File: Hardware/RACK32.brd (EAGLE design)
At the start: 120 x 54 mm, 95 parts, among them IC1 MCP9808-MSOP8, IC2 ESPWROOM32, IC3 LM358D, IC4 W5500-LQFP, IC5 CP2102N-A01-GQFN24, J1 SPI-LCD, J10 microSD, J11 IO, J2 I2CBR, J3 USB-C-16P-16P, J4 DC IN, J6 PWR_LED, Q1 FDN340P, Q2 MMDT3904, U1 HY931147C-RJ45

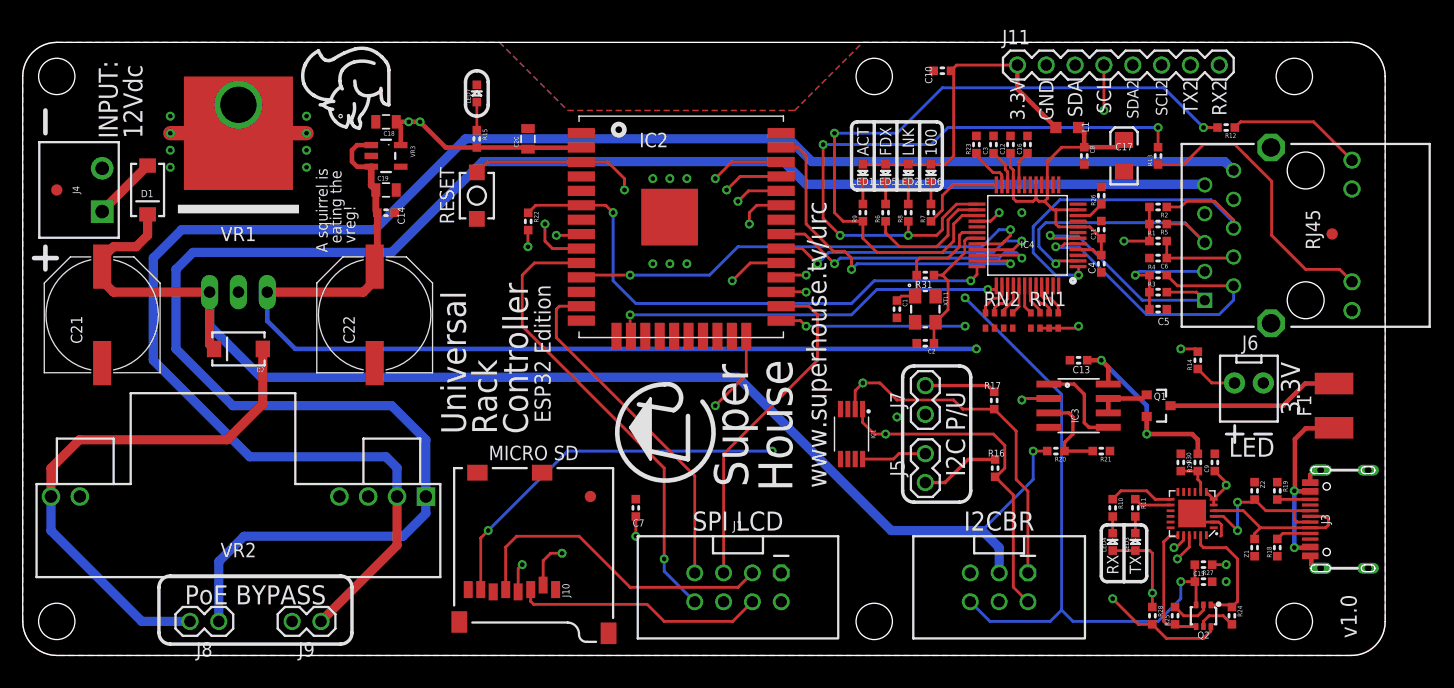
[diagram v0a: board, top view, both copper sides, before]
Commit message: Changed PTC to 1206 size. Replaced power LED header.
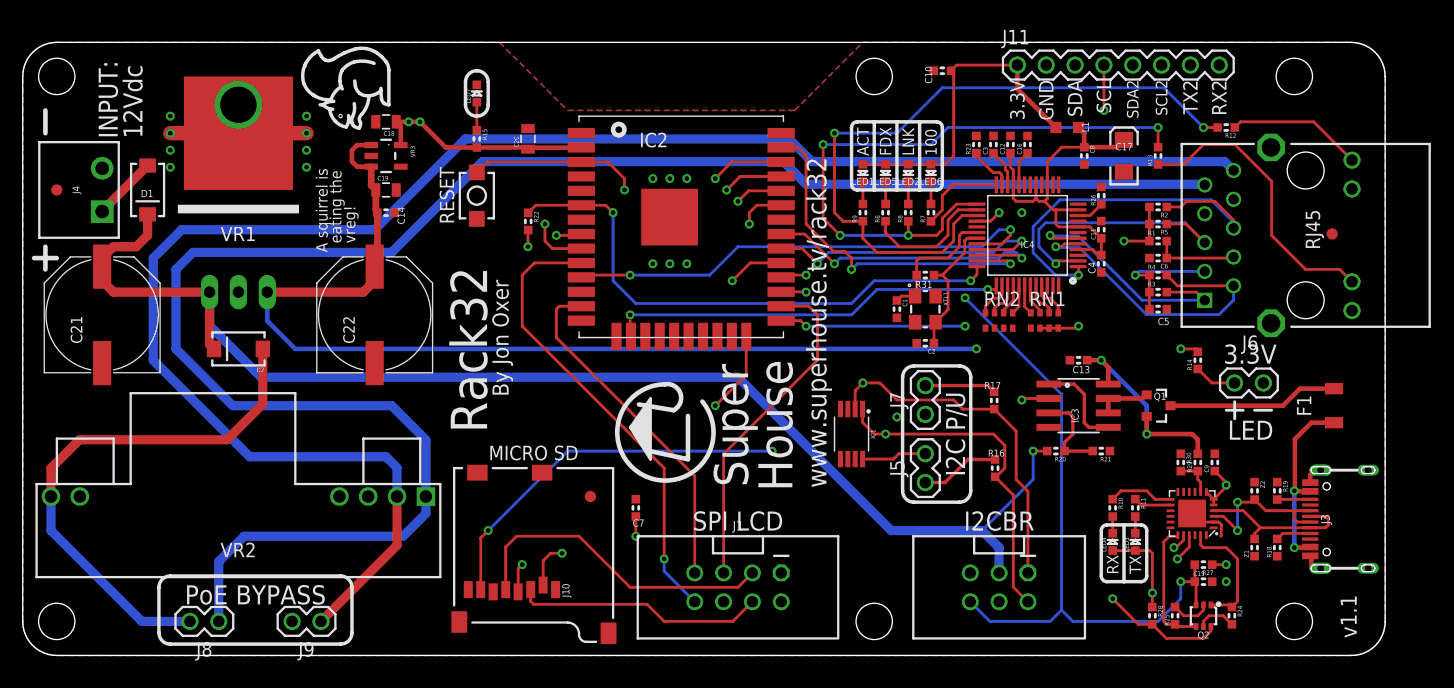
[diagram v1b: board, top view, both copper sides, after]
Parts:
- F1: value 500mA 1812 PTC -> 500mA 1206 PTC; device SuperHouse-Fuses:1812 -> SuperHouse-Fuses:1206
- J6: device SuperHouse-Connectors:1X02-KF2510 -> SuperHouse-Connectors:1X02-P
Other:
- board text added: "By Jon Oxer"
- board text added: "Rack32"
- board text added: "Rack32 v1.1 Mechanical Outline"
- board text added: "v1.1"
- board text added: "www.superhouse.tv/rack32"
- board text removed: "ESP32 Edition"
- board text removed: "Universal Rack Controller"
- board text removed: "Universal Rack Controller PCB v1.0 Mechanical Outline"
- board text removed: "v1.0"
- board text removed: "www.superhouse.tv/urc"
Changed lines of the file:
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@@
 <setting verticaltext="up"/>
 </settings>
-<grid distance="0.1" unitdist="mm" unit="mm" style="dots" multiple="1" display="no" altdistance="0.001" altunitdist="inch" altunit="inch"/>
+<grid distance="1" unitdist="mm" unit="mm" style="dots" multiple="1" display="no" altdistance="0.001" altunitdist="inch" altunit="inch"/>
 <layers>
 <layer number="1" name="Top" color="59" fill="1" visible="yes" active="yes"/>
@@
 <layer number="19" name="Unrouted" color="12" fill="1" visible="yes" active="yes"/>
 <layer number="20" name="Dimension" color="15" fill="1" visible="no" active="yes"/>
-<layer number="21" name="tPlace" color="58" fill="1" visible="no" active="yes"/>
-<layer number="22" name="bPlace" color="14" fill="1" visible="no" active="yes"/>
+<layer number="21" name="tPlace" color="58" fill="1" visible="yes" active="yes"/>
+<layer number="22" name="bPlace" color="14" fill="1" visible="yes" active="yes"/>
 <layer number="23" name="tOrigins" color="15" fill="1" visible="yes" active="yes"/>
 <layer number="24" name="bOrigins" color="15" fill="1" visible="yes" active="yes"/>
@@
 <text x="10.546" y="45.524" size="1.6764" layer="21" font="vector" ratio="17" distance="30" rot="R90">INPUT:
 12Vdc</text>
-<text x="70.792" y="14.754" size="1.7272" layer="21" font="vector" ratio="17" rot="SR90">www.superhouse.tv/urc</text>
+<text x="70.792" y="14.754" size="1.7272" layer="21" font="vector" ratio="17" rot="SR90">www.superhouse.tv/rack32</text>
 <hole x="112" y="51" drill="3.2"/>
 <hole x="112" y="3" drill="3.2"/>
@@
 <wire x1="13" y1="1" x2="28" y2="1" width="0.3048" layer="21"/>
 <text x="38" y="40.5" size="1.27" layer="21" font="vector" ratio="15" rot="SR90" align="bottom-center">RESET</text>
-<text x="46.5" y="20.5" size="1.4224" layer="21" font="vector" ratio="17" rot="R90">ESP32 Edition</text>
-<text x="44.5" y="19.5" size="2.1844" layer="21" font="vector" ratio="17" distance="25" rot="SR90">Universal
-Rack
-Controller</text>
-<text x="117.5" y="1.524" size="1.4224" layer="21" font="vector" ratio="17" rot="R90">v1.0</text>
+<text x="40.9" y="19.6" size="3.2" layer="21" font="vector" ratio="17" distance="25" rot="SR90">Rack32</text>
+<text x="117.5" y="1.524" size="1.4224" layer="21" font="vector" ratio="17" rot="R90">v1.1</text>
 <text x="64.27" y="4" size="1.016" layer="22" ratio="18" rot="SMR90" align="center-right">COPI</text>
 <text x="66.81" y="4" size="1.016" layer="22" ratio="18" rot="SMR90" align="center-right">3.3V</text>
@@
   eating the
   vreg!</text>
-<text x="108.25" y="17.5" size="1.6764" layer="21" font="vector" ratio="17" align="bottom-center">LED</text>
-<wire x1="106" y1="19.5" x2="107.5" y2="19.5" width="0.254" layer="21"/>
-<wire x1="106.75" y1="20.25" x2="106.75" y2="18.75" width="0.254" layer="21"/>
-<wire x1="108.5" y1="19.5" x2="110" y2="19.5" width="0.254" layer="21"/>
-<text x="112.5" y="23.5" size="1.6764" layer="21" font="vector" ratio="17" rot="R90" align="bottom-center">3.3V</text>
+<text x="108.15" y="19" size="1.6764" layer="21" font="vector" ratio="17" align="bottom-center">LED</text>
+<wire x1="106" y1="21.6" x2="107.5" y2="21.6" width="0.254" layer="21"/>
+<wire x1="106.75" y1="22.35" x2="106.75" y2="20.85" width="0.254" layer="21"/>
+<wire x1="108.5" y1="21.6" x2="110" y2="21.6" width="0.254" layer="21"/>
+<text x="108.1" y="25.7" size="1.6764" layer="21" font="vector" ratio="17" align="bottom-center">3.3V</text>
 <wire x1="32.25" y1="48.5" x2="32.25" y2="51.55" width="0.3048" layer="21"/>
 <wire x1="32.25" y1="51.55" x2="32" y2="52.3" width="0.3048" layer="21" curve="36.869898"/>
@@
 <dimension x1="63" y1="-1" x2="45" y2="-1" x3="54" y3="-3" textsize="1.778" layer="47"/>
 <dimension x1="45" y1="-1" x2="0" y2="-1" x3="22.5" y3="-3" textsize="1.778" layer="47"/>
-<text x="29" y="64" size="1.778" layer="47">Universal Rack Controller PCB v1.0 Mechanical Outline</text>
+<text x="29" y="64" size="1.778" layer="47">Rack32 v1.1 Mechanical Outline</text>
+<text x="42.8" y="22.8" size="1.4224" layer="21" font="vector" ratio="17" distance="25" rot="SR90">By Jon Oxer</text>
 </plain>
 <attributes>
@@
 <element name="R31" library="SuperHouse-Resistors" library_urn="urn:adsk.eagle:library:28961094" package="R0603" package3d_urn="urn:adsk.eagle:package:28961141/1" value="1M" x="79.5" y="33.5" smashed="yes" rot="R180">
 <attribute name="NAME" x="80.135" y="32.992" size="0.635" layer="25" font="vector" ratio="17" rot="R180"/>
-<attribute name="VALUE" x="80.516" y="34.4652" size="0.635" layer="27" font="vector" ratio="17" rot="R180"/>
+<attribute name="VALUE" x="78.984" y="34.1348" size="0.635" layer="27" font="vector" ratio="17"/>
 </element>
 <element name="LED1" library="SuperHouse-LEDs" library_urn="urn:adsk.eagle:library:11790571" package="LED-0603" package3d_urn="urn:adsk.eagle:package:7066240/3" value="GREEN" x="74" y="42.5" smashed="yes" rot="R270">
@@
 <element name="C13" library="SuperHouse-Capacitors" library_urn="urn:adsk.eagle:library:28961179" package="C0603" package3d_urn="urn:adsk.eagle:package:7066315/6" value="100nF" x="93" y="26" smashed="yes" rot="R180">
 <attribute name="NAME" x="94.016" y="25.492" size="0.635" layer="25" font="vector" ratio="17" rot="R180"/>
-<attribute name="VALUE" x="94.016" y="27.143" size="0.635" layer="27" font="vector" ratio="17" rot="R180"/>
+<attribute name="VALUE" x="94.716" y="27.243" size="0.635" layer="27" font="vector" ratio="17" rot="R180"/>
 </element>
 <element name="Q1" library="SuperHouse-Transistors" library_urn="urn:adsk.eagle:library:28961147" package="SOT23-3" package3d_urn="urn:adsk.eagle:package:28961169/1" value="FDN340P" x="100" y="22" smashed="yes" rot="R270">
@@
 <attribute name="VALUE" x="30.984" y="47.903" size="0.8128" layer="27"/>
 </element>
-<element name="F1" library="SuperHouse-Fuses" library_urn="urn:adsk.eagle:library:11769263" package="1812" package3d_urn="urn:adsk.eagle:package:11769373/4" value="500mA 1812 PTC" x="115.5" y="22" smashed="yes" rot="R90">
+<element name="F1" library="SuperHouse-Fuses" library_urn="urn:adsk.eagle:library:11769263" package="1206" package3d_urn="urn:adsk.eagle:package:30910324/2" value="500mA 1206 PTC" x="115.5" y="22" smashed="yes" rot="R90">
 <attribute name="NAME" x="113.5" y="22" size="1.27" layer="25" rot="R90" align="bottom-center"/>
 <attribute name="VALUE" x="117.5" y="22" size="1.27" layer="27" rot="R90" align="top-center"/>
@@
 <attribute name="VALUE" x="5.73" y="41" size="0.6096" layer="27" rot="R90" align="bottom-center"/>
 </element>
-<element name="J6" library="SuperHouse-Connectors" library_urn="urn:adsk.eagle:library:11765989" package="1X02-KF2510" package3d_urn="urn:adsk.eagle:package:15401905/4" value="PWR_LED" x="108" y="24" smashed="yes">
+<element name="J6" library="SuperHouse-Connectors" library_urn="urn:adsk.eagle:library:11765989" package="1X02-P" package3d_urn="urn:adsk.eagle:package:11816162/4" value="PWR_LED" x="108" y="24" smashed="yes">
 <attribute name="NAME" x="108.1138" y="26.9088" size="1.27" layer="25" ratio="10" align="bottom-center"/>
 <attribute name="VALUE" x="108.19" y="19.015" size="1.27" layer="27" align="bottom-center"/>
@@
 <contactref element="Q1" pad="3"/>
 <contactref element="F1" pad="2"/>
-<wire x1="115.5" y1="23.95" x2="112.95" y2="23.95" width="0.4064" layer="1"/>
-<wire x1="111" y1="22" x2="101.1" y2="22" width="0.4064" layer="1"/>
-<wire x1="112.95" y1="23.95" x2="111" y2="22" width="0.4064" layer="1"/>
+<wire x1="101.1" y1="22" x2="111" y2="22" width="0.4064" layer="1"/>
+<wire x1="111" y1="22" x2="112.5" y2="23.5" width="0.4064" layer="1"/>
+<wire x1="112.5" y1="23.5" x2="115.5" y2="23.5" width="0.4064" layer="1"/>
 </signal>
 <signal name="N$12">
@@
 <wire x1="113.355" y1="9.5" x2="112" y2="9.5" width="0.4064" layer="1"/>
 <wire x1="112" y1="9.5" x2="112" y2="14.5" width="0.4064" layer="16"/>
-<wire x1="115.5" y1="20.05" x2="115.45" y2="20" width="0.4064" layer="1"/>
-<wire x1="112.05" y1="19.05" x2="112.05" y2="14.45" width="0.4064" layer="1"/>
-<wire x1="115.45" y1="20" x2="113" y2="20" width="0.4064" layer="1"/>
-<wire x1="113" y1="20" x2="112.05" y2="19.05" width="0.4064" layer="1"/>
+<wire x1="112.05" y1="14.45" x2="112.05" y2="19.05" width="0.4064" layer="1"/>
+<wire x1="113.5" y1="20.5" x2="115.5" y2="20.5" width="0.4064" layer="1"/>
+<wire x1="112.05" y1="19.05" x2="113.5" y2="20.5" width="0.4064" layer="1"/>
 </signal>
 <signal name="N$4">

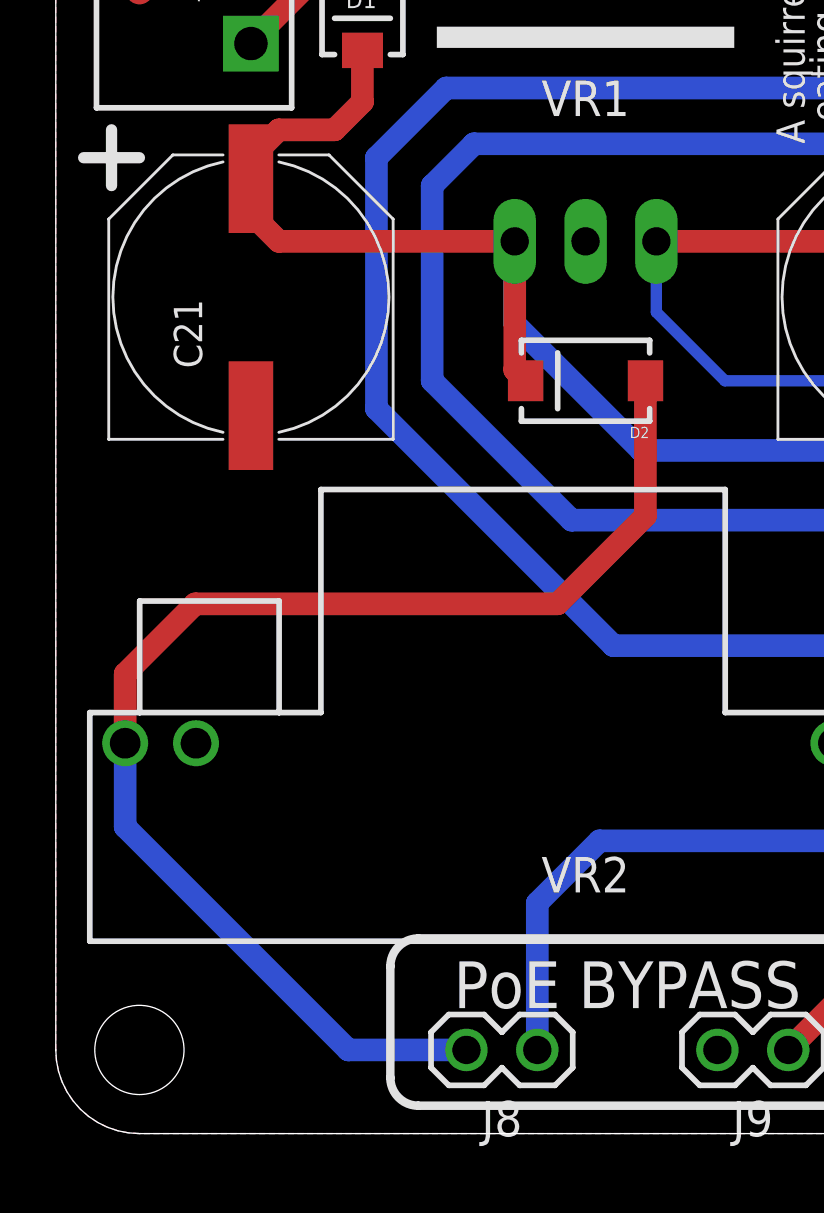
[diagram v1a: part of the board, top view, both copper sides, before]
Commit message: Added backpower protection for PoE module.
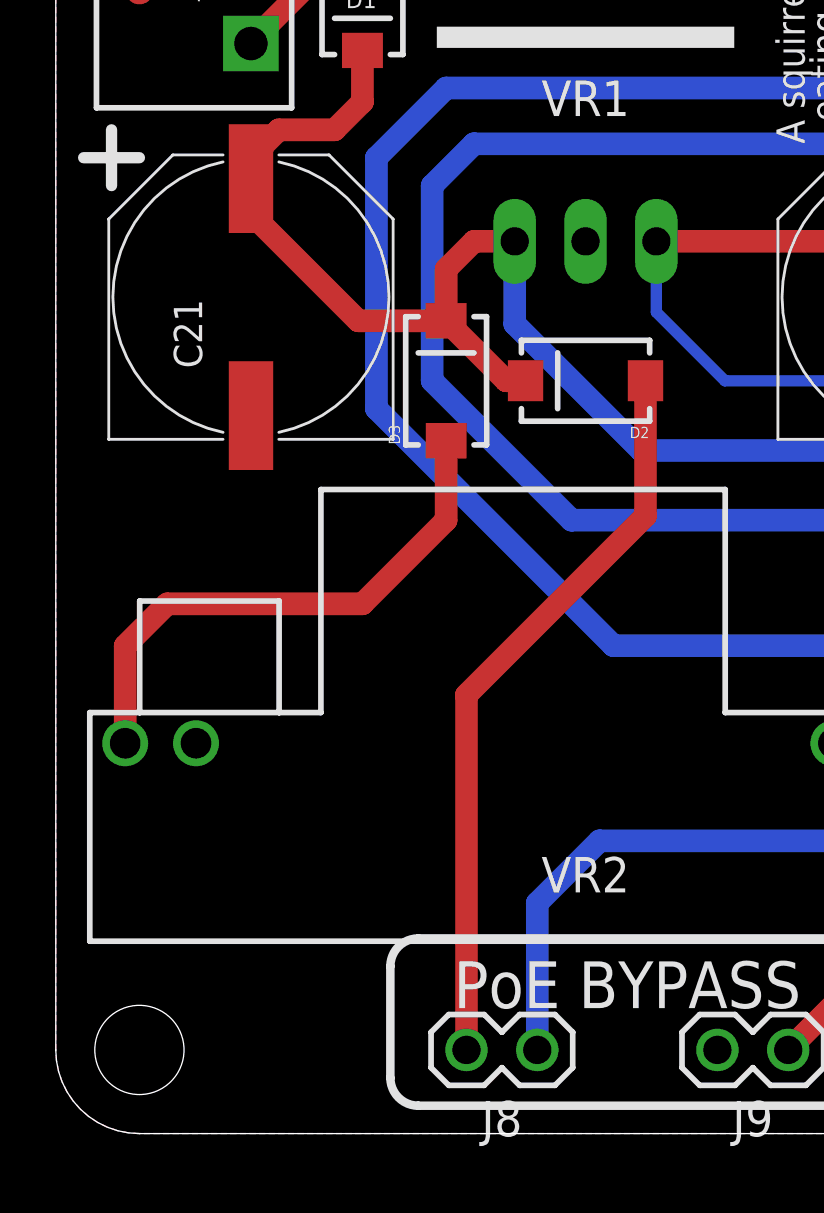
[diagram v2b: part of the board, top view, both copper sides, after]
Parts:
- added D3: SS56, SuperHouse-Diodes:SMA-DIODE
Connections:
- new net N$13: D3.A, VR2.6
- net 12V: now also D3.C
- net N$8: no longer VR2.6
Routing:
- net N$8: track 46.9 -> 26.7 mm
- net N$13: track 0.00 -> 19.7 mm
- net 12V: track 116.6 -> 118.7 mm
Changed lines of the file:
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@@
 <layer number="14" name="Route14" color="1" fill="6" visible="no" active="no"/>
 <layer number="15" name="Route15" color="4" fill="1" visible="no" active="yes"/>
-<layer number="16" name="Bottom" color="9" fill="1" visible="no" active="yes"/>
+<layer number="16" name="Bottom" color="9" fill="1" visible="yes" active="yes"/>
 <layer number="17" name="Pads" color="2" fill="1" visible="yes" active="yes"/>
 <layer number="18" name="Vias" color="2" fill="1" visible="yes" active="yes"/>
@@
 <attribute name="VALUE" x="86.34" y="48.825" size="1.27" layer="27"/>
 </element>
+<element name="D3" library="SuperHouse-Diodes" library_urn="urn:adsk.eagle:library:28961057" package="SMA-DIODE" package3d_urn="urn:adsk.eagle:package:28961089/1" value="SS56" x="14" y="27" smashed="yes" rot="R90">
+<attribute name="NAME" x="12.349" y="24.714" size="0.4064" layer="25" rot="R90"/>
+<attribute name="VALUE" x="12.349" y="27.254" size="0.4064" layer="27" rot="R90"/>
+</element>
 </elements>
 <signals>
@@
 <signal name="N$8">
 <contactref element="J8" pad="2"/>
-<contactref element="VR2" pad="6"/>
 <contactref element="D2" pad="A"/>
 <wire x1="21.15" y1="27" x2="21.15" y2="22.15" width="0.8128" layer="1"/>
-<wire x1="21.15" y1="22.15" x2="18" y2="19" width="0.8128" layer="1"/>
-<wire x1="18" y1="19" x2="5" y2="19" width="0.8128" layer="1"/>
-<wire x1="5" y1="19" x2="2.49" y2="16.49" width="0.8128" layer="1"/>
-<wire x1="2.49" y1="16.49" x2="2.49" y2="14" width="0.8128" layer="1"/>
-<wire x1="2.49" y1="14" x2="2.49" y2="11" width="0.8128" layer="16"/>
-<wire x1="2.49" y1="11" x2="10.49" y2="3" width="0.8128" layer="16"/>
-<wire x1="10.49" y1="3" x2="14.73" y2="3" width="0.8128" layer="16"/>
+<wire x1="14.73" y1="15.73" x2="14.73" y2="3" width="0.8128" layer="1"/>
+<wire x1="21.15" y1="22.15" x2="14.73" y2="15.73" width="0.8128" layer="1"/>
 </signal>
 <signal name="12V">
@@
 <contactref element="VR1" pad="1"/>
 <contactref element="C21" pad="+"/>
-<wire x1="16.46" y1="32" x2="16.46" y2="27.39" width="0.8128" layer="1"/>
-<wire x1="16.46" y1="27.39" x2="16.85" y2="27" width="0.8128" layer="1"/>
-<wire x1="16.46" y1="32" x2="8" y2="32" width="0.8128" layer="1"/>
-<wire x1="8" y1="32" x2="7" y2="33" width="0.8128" layer="1"/>
-<wire x1="7" y1="33" x2="7" y2="34.25" width="0.8128" layer="1"/>
+<wire x1="7" y1="34.25" x2="7" y2="33" width="0.8128" layer="1"/>
 <wire x1="11" y1="38.85" x2="11" y2="37" width="0.8128" layer="1"/>
 <wire x1="11" y1="37" x2="10" y2="36" width="0.8128" layer="1"/>
@@
 <wire x1="89" y1="18" x2="89" y2="15.5" width="0.254" layer="16"/>
 <wire x1="89" y1="15.5" x2="84.5" y2="11" width="0.254" layer="16"/>
+<contactref element="D3" pad="C"/>
+<wire x1="10.85" y1="29.15" x2="14" y2="29.15" width="0.8128" layer="1"/>
+<wire x1="7" y1="33" x2="10.85" y2="29.15" width="0.8128" layer="1"/>
+<wire x1="16.85" y1="27" x2="16.15" y2="27" width="0.8128" layer="1"/>
+<wire x1="16.15" y1="27" x2="14" y2="29.15" width="0.8128" layer="1"/>
+<wire x1="14" y1="29.15" x2="14" y2="31" width="0.8128" layer="1"/>
+<wire x1="14" y1="31" x2="15" y2="32" width="0.8128" layer="1"/>
+<wire x1="15" y1="32" x2="16.46" y2="32" width="0.8128" layer="1"/>
 </signal>
 <signal name="VB1">
@@
 <wire x1="105.39" y1="45.89" x2="105.39" y2="52" width="0.254" layer="15"/>
 </signal>
+<signal name="N$13">
+<contactref element="VR2" pad="6"/>
+<contactref element="D3" pad="A"/>
+<wire x1="2.49" y1="14" x2="2.49" y2="17.49" width="0.8128" layer="1"/>
+<wire x1="2.49" y1="17.49" x2="4" y2="19" width="0.8128" layer="1"/>
+<wire x1="4" y1="19" x2="11" y2="19" width="0.8128" layer="1"/>
+<wire x1="11" y1="19" x2="14" y2="22" width="0.8128" layer="1"/>
+<wire x1="14" y1="22" x2="14" y2="24.85" width="0.8128" layer="1"/>
+</signal>
 </signals>
